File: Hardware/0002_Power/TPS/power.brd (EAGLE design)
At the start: 160 x 100 mm, 16 parts

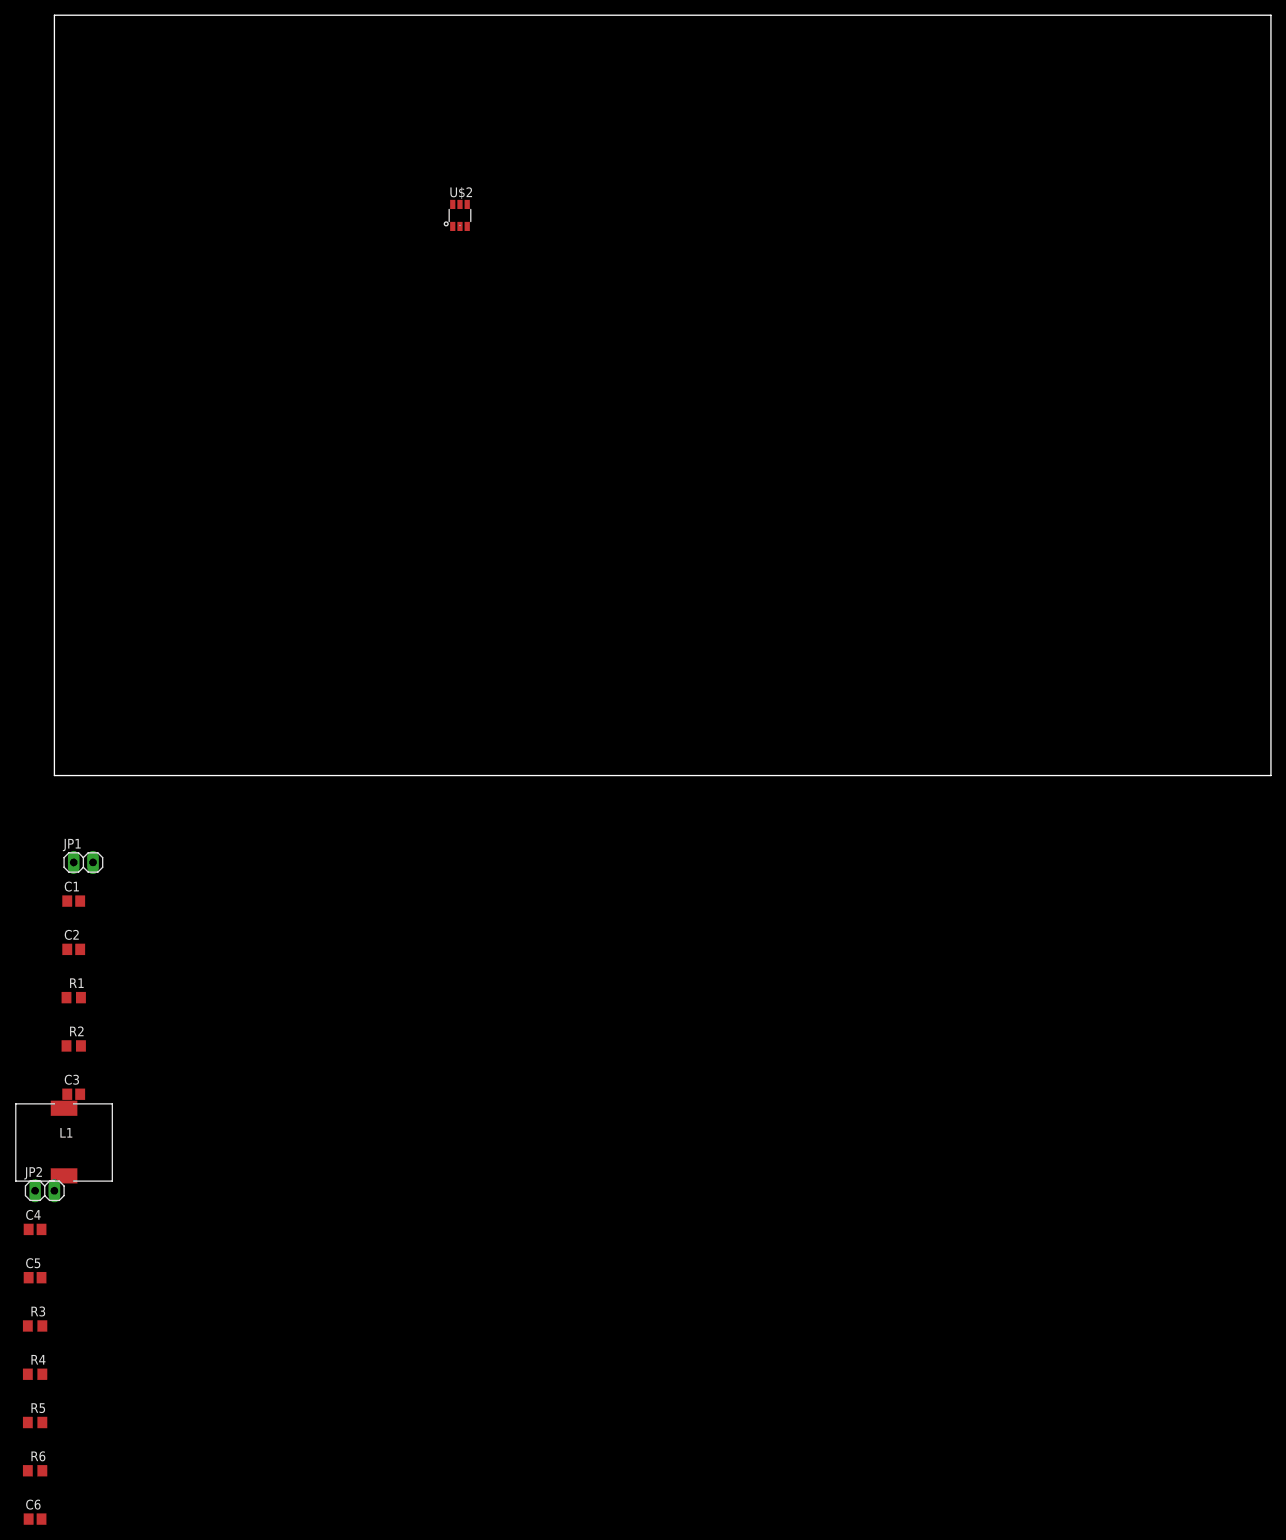
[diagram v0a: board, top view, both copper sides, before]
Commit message: RF power updated schematic & board (in progress)
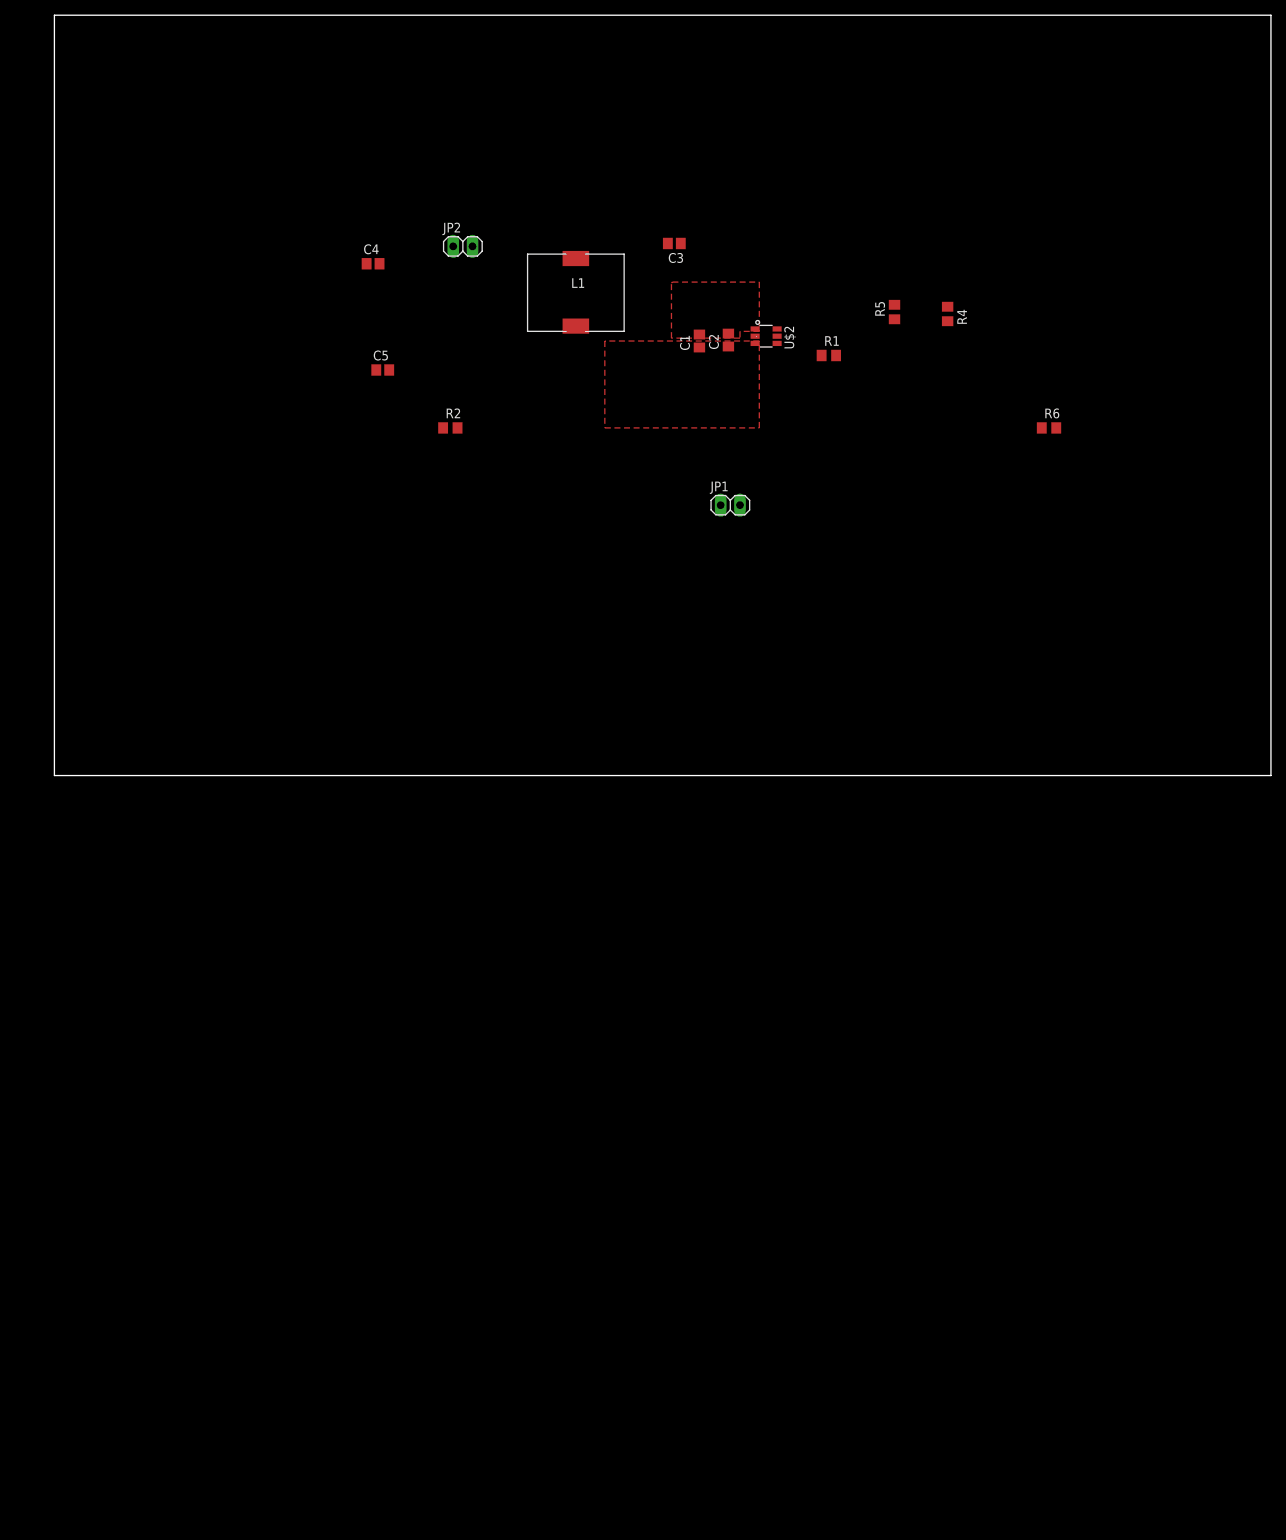
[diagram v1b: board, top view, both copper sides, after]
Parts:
- removed C6: 75pF, rcl:C2012
- removed R3: 49.9, rcl:R0805
- moved R6 191.3 mm to (130.8, 45.7)
- moved R5 184.7 mm to (110.5, 61.0), turned to 90 degrees
- moved R4 184.0 mm to (117.5, 60.7), turned to 270 degrees
- moved C3 137.0 mm to (81.5, 70.0), turned to 180 degrees
- moved JP2 135.8 mm to (53.7, 69.6)
- moved C4 134.6 mm to (41.9, 67.3)
- moved L1 130.5 mm to (68.6, 63.5)
- moved R1 130.4 mm to (101.9, 55.2)
- moved C5 127.8 mm to (43.2, 53.3)
- moved C2 117.6 mm to (88.6, 57.3), turned to 90 degrees
- moved C1 110.4 mm to (84.8, 57.1), turned to 90 degrees
- moved JP1 97.2 mm to (88.9, 35.6)
- moved R2 95.2 mm to (52.1, 45.7)
- moved U$2 43.3 mm to (93.6, 57.8), turned to 270 degrees
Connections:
- net N$4: no longer R3.2
- net N$5: no longer R3.1
- net N$7: no longer C6.1
- net N$8: no longer C6.2
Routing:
- added copper zone on layer 1, net +12V
- added copper zone on layer 1, net GND
